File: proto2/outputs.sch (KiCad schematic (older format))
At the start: 36 parts, among them U1 AQY282SX, U10 AQY282SX, U11 AQY282SX, U12 AQY282SX, U2 AQY282SX, U3 AQY282SX, U4 AQY282SX, U5 AQY282SX, U6 AQY282SX, U7 AQY282SX, U8 AQY282SX, U9 AQY282SX

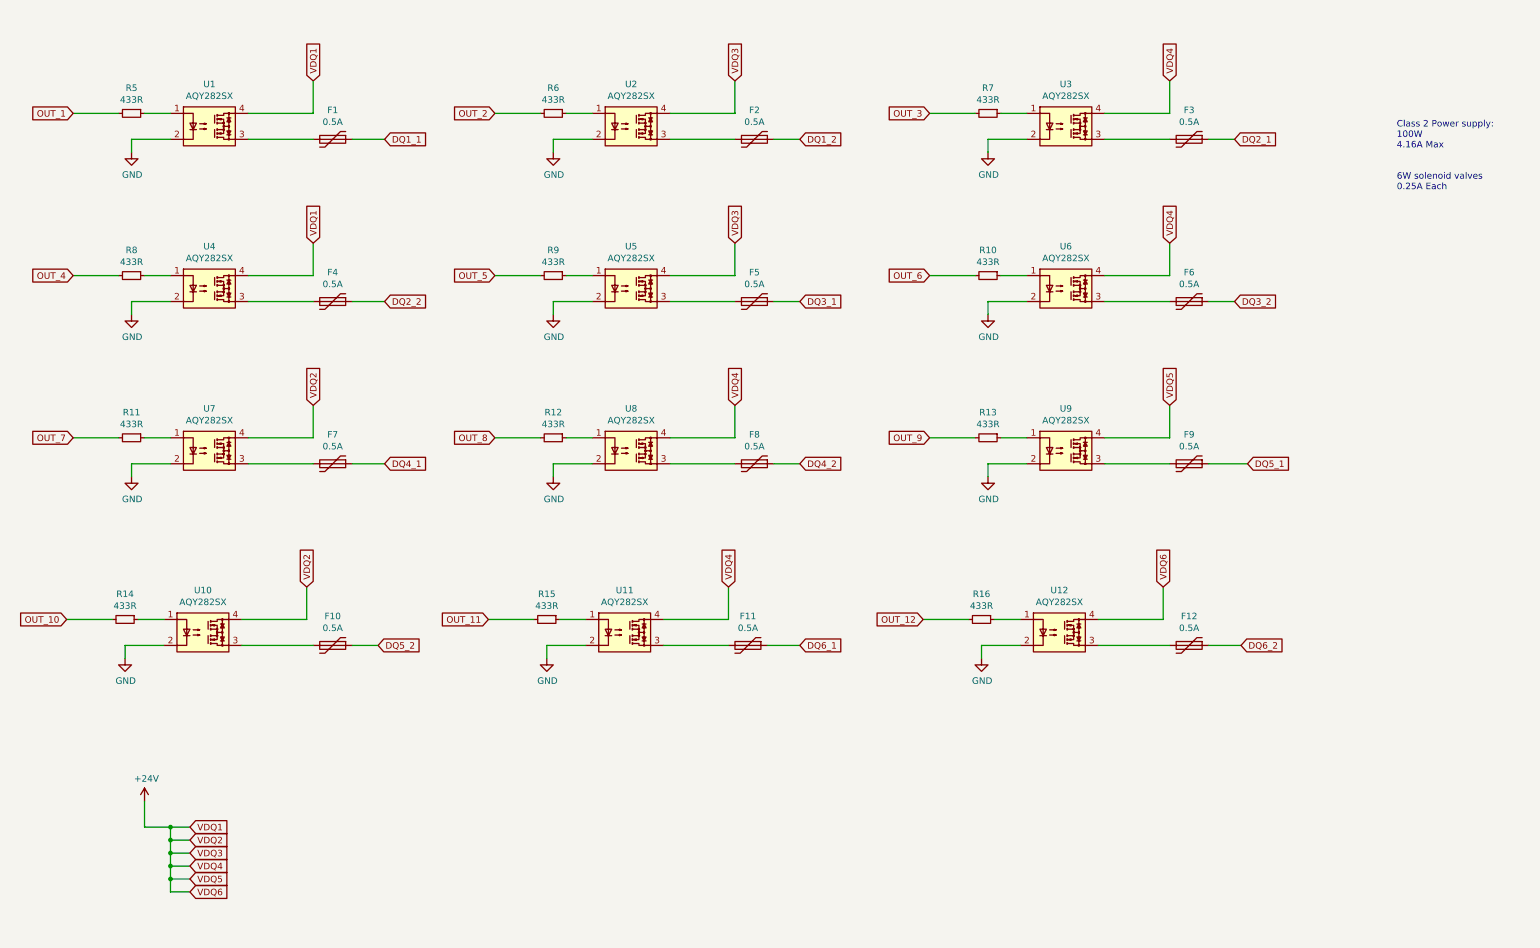
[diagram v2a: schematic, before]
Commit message: Added MOSFET drivers for the SSRs, pullups for I2C, and referenced DIP switches to 3V3.
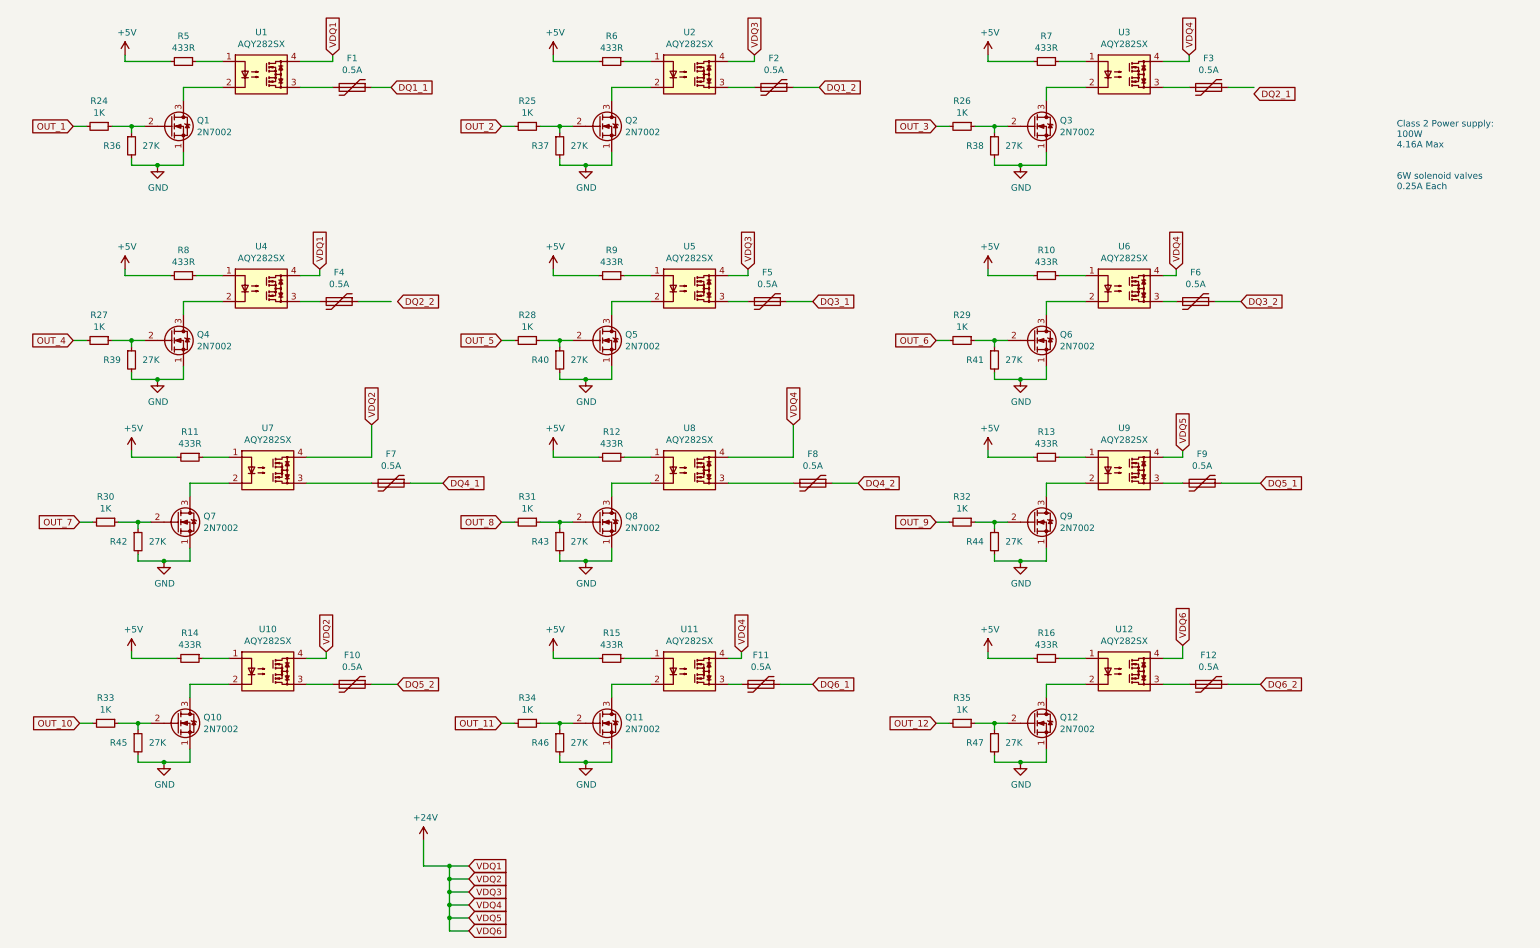
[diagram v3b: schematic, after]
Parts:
- added Q1, Q10, Q11, Q12, Q2, Q3, Q4, Q5, Q6, Q7, Q8, Q9: 2N7002, Package_TO_SOT_SMD:SOT-23, symbol Transistor_FET:2N7000
- added R24, R25, R26, R27, R28, R29, R30, R31, R32, R33, R34, R35: 1K, Resistor_SMD:R_0805_2012Metric, symbol Device:R_Small
- added R36, R37, R38, R39, R40, R41, R42, R43, R44, R45, R46, R47: 27K, Resistor_SMD:R_0805_2012Metric, symbol Device:R_Small
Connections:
- net DQ2_1: no longer F3.1
- net DQ2_2: no longer F4.1
- net GND: now also Q1.1 (S), Q10.1 (S), Q11.1 (S), Q12.1 (S), Q2.1 (S), Q3.1 (S), Q4.1 (S), Q5.1 (S), Q6.1 (S), Q7.1 (S), Q8.1 (S), Q9.1 (S), R36.2, R37.2, R38.2, R39.2, R40.2, R41.2, R42.2, R43.2, R44.2, R45.2, R46.2, R47.2; no longer U1.2, U10.2, U11.2, U12.2, U2.2, U3.2, U4.2, U5.2, U6.2, U7.2, U8.2, U9.2
- net OUT_1: now also R24.2; no longer R5.2
- net OUT_10: now also R33.2; no longer R14.2
- net OUT_11: now also R34.2; no longer R15.2
- net OUT_12: now also R35.2; no longer R16.2
- net OUT_2: now also R25.2; no longer R6.2
- net OUT_3: now also R26.2; no longer R7.2
- net OUT_4: now also R27.2; no longer R8.2
- net OUT_5: now also R28.2; no longer R9.2
- net OUT_6: now also R29.2; no longer R10.2
- net OUT_7: now also R30.2; no longer R11.2
- net OUT_8: now also R31.2; no longer R12.2
- net OUT_9: now also R32.2; no longer R13.2
- new net: Q1.3 (D), U1.2
- new net: Q4.3 (D), U4.2
- new net: Q7.3 (D), U7.2
- new net: Q10.3 (D), U10.2
- new net: Q2.3 (D), U2.2
- new net: Q5.3 (D), U5.2
- new net: Q8.3 (D), U8.2
- new net: Q11.3 (D), U11.2
- new net: Q3.3 (D), U3.2
- new net: Q6.3 (D), U6.2
- new net: Q9.3 (D), U9.2
- new net: Q12.3 (D), U12.2
- new net: Q1.2 (G), R24.1, R36.1
- new net: Q2.2 (G), R25.1, R37.1
- new net: Q3.2 (G), R26.1, R38.1
- new net: Q4.2 (G), R27.1, R39.1
- new net: Q5.2 (G), R28.1, R40.1
- new net: Q8.2 (G), R31.1, R43.1
- new net: Q6.2 (G), R29.1, R41.1
- new net: Q9.2 (G), R32.1, R44.1
- new net: Q7.2 (G), R30.1, R42.1
- new net: Q12.2 (G), R35.1, R47.1
- new net: Q11.2 (G), R34.1, R46.1
- new net: Q10.2 (G), R33.1, R45.1
- new net +5V: R10.2, R11.2, R12.2, R13.2, R14.2, R15.2, R16.2, R5.2, R6.2, R7.2, R8.2, R9.2
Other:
- moved on the sheet: F1, F10, F11, F12, F2, F3, F4, F5, F6, F7, F8, F9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

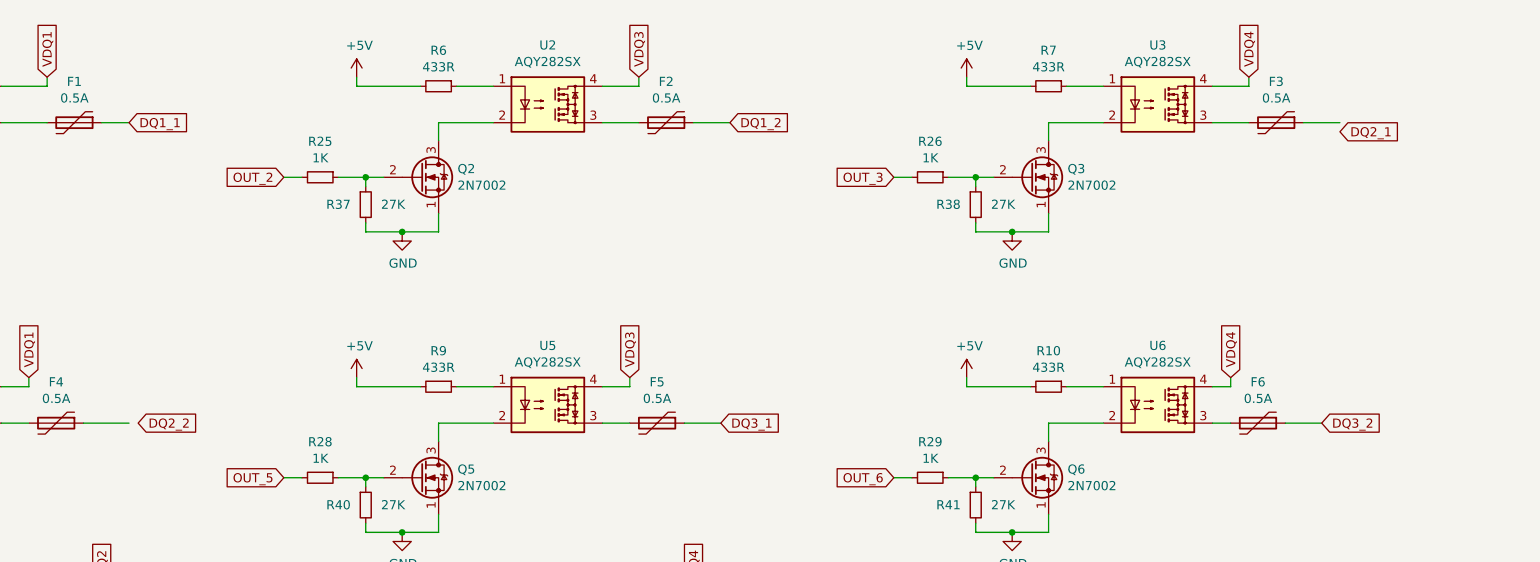
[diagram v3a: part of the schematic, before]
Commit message: Removed Raspberry Pi, added spacing to terminals.
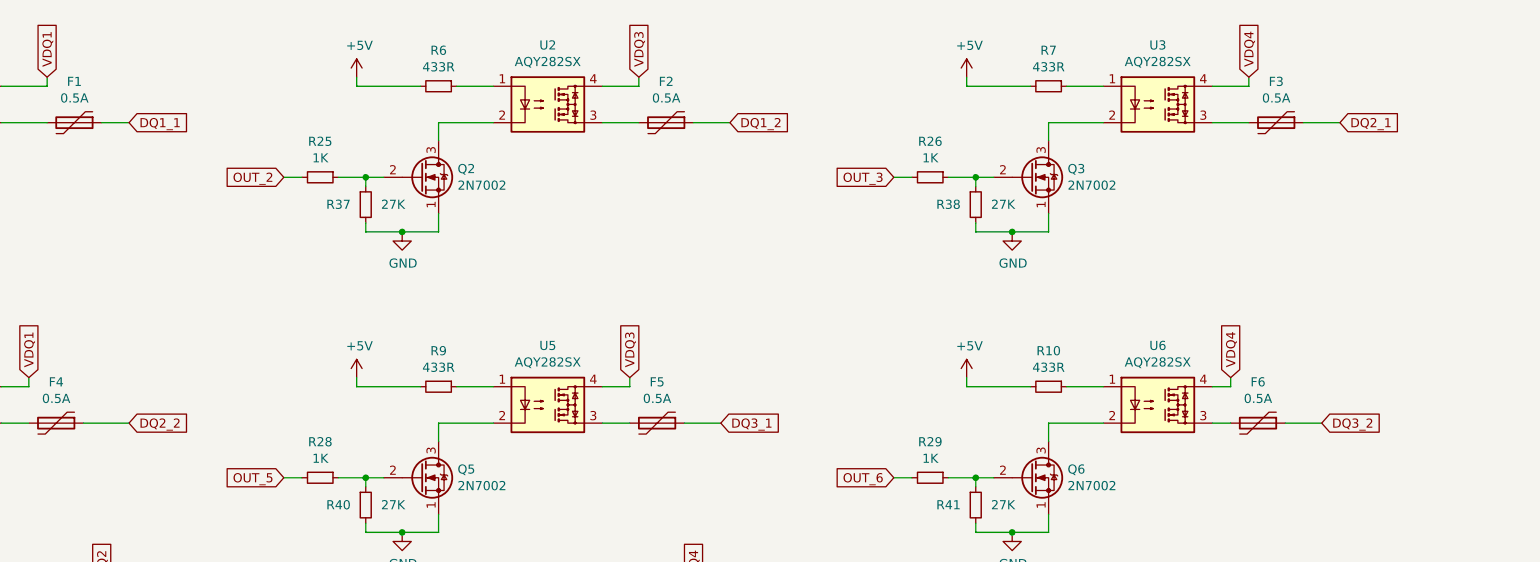
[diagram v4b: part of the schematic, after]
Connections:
- net DQ2_1: now also F3.1
- net DQ2_2: now also F4.1
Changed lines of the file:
@@
 Wire Wire Line
 	2750 4250 3250 4250
-Text GLabel 10050 1250 2    50   Input ~ 0
+Text GLabel 10050 1200 2    50   Input ~ 0
 DQ2_1
 Text GLabel 7600 1500 0    50   Input ~ 0
@@
 Wire Wire Line
 	2750 5800 2950 5800
-Text GLabel 3450 2850 2    50   Input ~ 0
+Text GLabel 3400 2850 2    50   Input ~ 0
 DQ2_2
 Text GLabel 950  3150 0    50   Input ~ 0

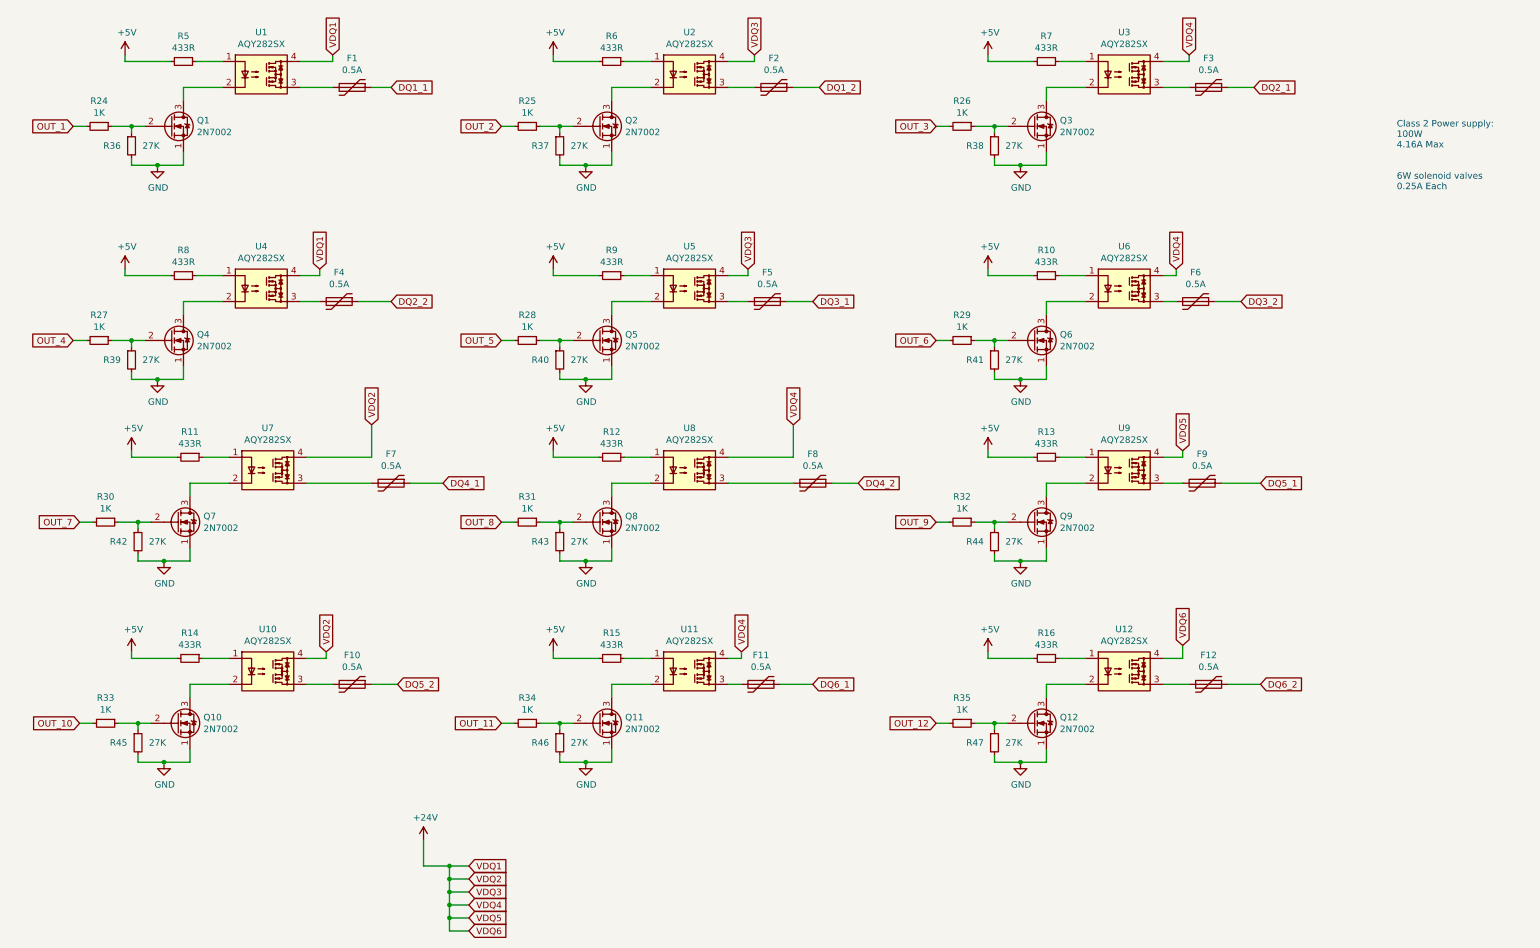
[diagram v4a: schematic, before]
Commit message: Replaced 2N7000 symbol with 2N7002.
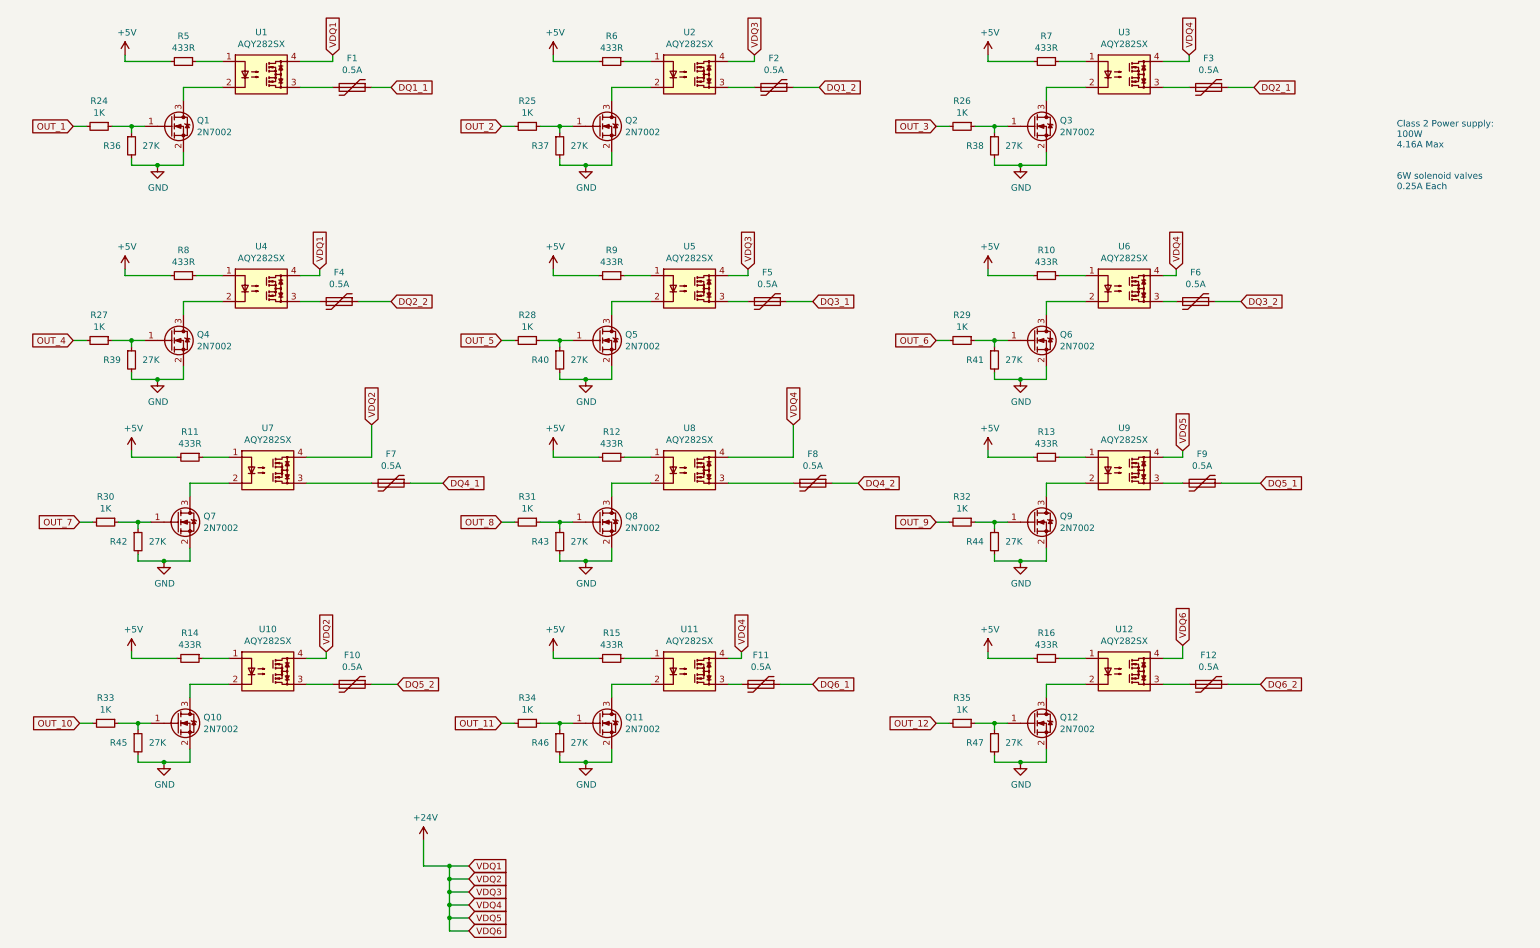
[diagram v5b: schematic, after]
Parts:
- removed Q1, Q10, Q11, Q12, Q2, Q3, Q4, Q5, Q6, Q7, Q8, Q9: 2N7002, Package_TO_SOT_SMD:SOT-23, symbol Transistor_FET:2N7000
- added Q1, Q10, Q11, Q12, Q2, Q3, Q4, Q5, Q6, Q7, Q8, Q9: 2N7002, Package_TO_SOT_SMD:SOT-23, symbol Transistor_FET:2N7002
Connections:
- net GND: now also Q1.2 (S), Q10.2 (S), Q11.2 (S), Q12.2 (S), Q2.2 (S), Q3.2 (S), Q4.2 (S), Q5.2 (S), Q6.2 (S), Q7.2 (S), Q8.2 (S), Q9.2 (S)
- net at U1.2: now also Q1.3 (D)
- net at U4.2: now also Q4.3 (D)
- net at U7.2: now also Q7.3 (D)
- net at U10.2: now also Q10.3 (D)
- net at U2.2: now also Q2.3 (D)
- net at U5.2: now also Q5.3 (D)
- net at U8.2: now also Q8.3 (D)
- net at U11.2: now also Q11.3 (D)
- net at U3.2: now also Q3.3 (D)
- net at U6.2: now also Q6.3 (D)
- net at U9.2: now also Q9.3 (D)
- net at U12.2: now also Q12.3 (D)
- net at R24.1, R36.1: now also Q1.1 (G)
- net at R25.1, R37.1: now also Q2.1 (G)
- net at R26.1, R38.1: now also Q3.1 (G)
- net at R27.1, R39.1: now also Q4.1 (G)
- net at R28.1, R40.1: now also Q5.1 (G)
- net at R31.1, R43.1: now also Q8.1 (G)
- net at R29.1, R41.1: now also Q6.1 (G)
- net at R32.1, R44.1: now also Q9.1 (G)
- net at R30.1, R42.1: now also Q7.1 (G)
- net at R35.1, R47.1: now also Q12.1 (G)
- net at R34.1, R46.1: now also Q11.1 (G)
- net at R33.1, R45.1: now also Q10.1 (G)
